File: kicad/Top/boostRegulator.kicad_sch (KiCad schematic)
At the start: 20 parts

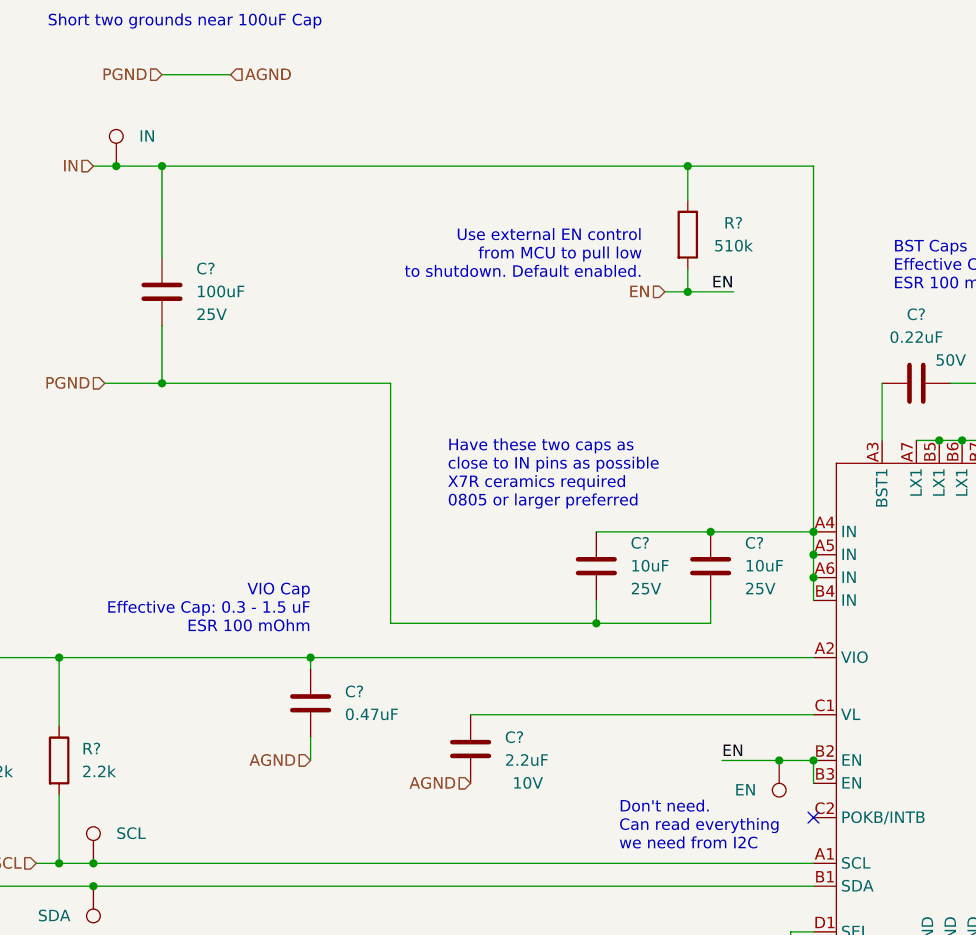
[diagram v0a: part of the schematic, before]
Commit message: Changed boost regulator to default off with MCU to turn on
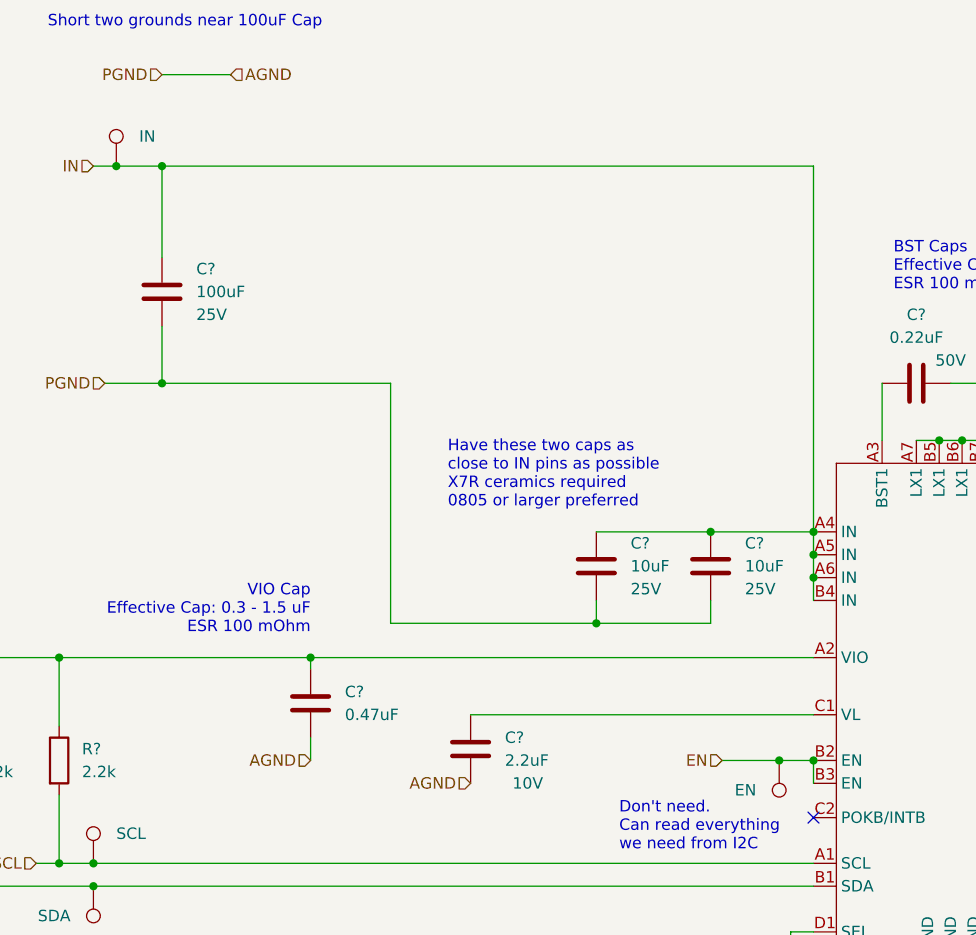
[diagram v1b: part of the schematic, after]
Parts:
- removed R?: 510k, symbol Device:R
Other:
- note removed: "Use external EN control from MCU to pull low to shutdown. Default enabled."
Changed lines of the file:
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@@
   (junction (at 160.02 85.09) (diameter 0) (color 0 0 0 0)
   )
-  (junction (at 132.08 68.58) (diameter 0) (color 0 0 0 0)
-  )
   (junction (at 193.04 100.33) (diameter 0) (color 0 0 0 0)
   )
@@
   )
   (junction (at 193.04 97.79) (diameter 0) (color 0 0 0 0)
-  )
-  (junction (at 132.08 54.61) (diameter 0) (color 0 0 0 0)
   )
   (junction (at 210.82 95.25) (diameter 0) (color 0 0 0 0)
@@
     (stroke (width 0) (type default) (color 0 0 0 0))
   )
-  (wire (pts (xy 132.08 66.04) (xy 132.08 68.58))
-    (stroke (width 0) (type default) (color 0 0 0 0))
-  )
   (wire (pts (xy 146.05 97.79) (xy 146.05 100.33))
     (stroke (width 0) (type default) (color 0 0 0 0))
@@
     (stroke (width 0) (type default) (color 0 0 0 0))
   )
-  (wire (pts (xy 132.08 68.58) (xy 137.16 68.58))
-    (stroke (width 0) (type default) (color 0 0 0 0))
-  )
   (wire (pts (xy 179.07 146.05) (xy 179.07 151.13))
     (stroke (width 0) (type default) (color 0 0 0 0))
   )
-  (wire (pts (xy 132.08 54.61) (xy 132.08 58.42))
-    (stroke (width 0) (type default) (color 0 0 0 0))
-  )
   (wire (pts (xy 146.05 54.61) (xy 146.05 95.25))
     (stroke (width 0) (type default) (color 0 0 0 0))
@@
     (stroke (width 0) (type default) (color 0 0 0 0))
   )
-  (wire (pts (xy 132.08 54.61) (xy 146.05 54.61))
-    (stroke (width 0) (type default) (color 0 0 0 0))
-  )
   (wire (pts (xy 99.06 105.41) (xy 121.92 105.41))
     (stroke (width 0) (type default) (color 0 0 0 0))
@@
     (stroke (width 0) (type default) (color 0 0 0 0))
   )
-  (wire (pts (xy 129.54 68.58) (xy 132.08 68.58))
-    (stroke (width 0) (type default) (color 0 0 0 0))
-  )
   (wire (pts (xy 62.23 116.84) (xy 62.23 109.22))
     (stroke (width 0) (type default) (color 0 0 0 0))
   )
-  (wire (pts (xy 73.66 54.61) (xy 132.08 54.61))
+  (wire (pts (xy 73.66 54.61) (xy 146.05 54.61))
     (stroke (width 0) (type default) (color 0 0 0 0))
   )
@@
     (effects (font (size 1.27 1.27)) (justify left bottom))
   )
-  (text "Use external EN control\nfrom MCU to pull low\nto shutdown. Default enabled."
-    (at 127 67.31 0)
-    (effects (font (size 1.27 1.27)) (justify right bottom))
-  )
   (text "1.08 to 2.0V" (at 34.29 107.95 0)
     (effects (font (size 1.27 1.27)) (justify left bottom))
@@
     (effects (font (size 1.27 1.27)) (justify right bottom))
   )
-  (label "EN" (at 137.16 68.58 180)
-    (effects (font (size 1.27 1.27)) (justify right bottom))
-  )
-  (label "EN" (at 135.89 120.65 0)
-    (effects (font (size 1.27 1.27)) (justify left bottom))
-  )
   (hierarchical_label "OUT" (shape input) (at 250.19 95.25 0)
     (effects (font (size 1.27 1.27)) (justify left))
@@
     (effects (font (size 1.27 1.27)) (justify right))
   )
-  (hierarchical_label "EN" (shape input) (at 129.54 68.58 180)
+  (hierarchical_label "EN" (shape input) (at 135.89 120.65 180)
     (effects (font (size 1.27 1.27)) (justify right))
   )
@@
     (pin "1")
   )
-  (symbol (lib_id "Device:R") (at 132.08 62.23 0) (unit 1)
-    (in_bom yes) (on_board yes)
-    (property "Reference" "R?" (id 0) (at 137.16 60.96 0))
-    (property "Value" "510k" (id 1) (at 137.16 63.5 0))
-    (property "Footprint" "" (id 2) (at 130.302 62.23 90)
-      (effects (font (size 1.27 1.27)) hide)
-    )
-    (property "Datasheet" "~" (id 3) (at 132.08 62.23 0)
-      (effects (font (size 1.27 1.27)) hide)
-    )
-    (pin "1")
-    (pin "2")
-  )
   (symbol (lib_id "Device:C") (at 107.95 119.38 0) (unit 1)

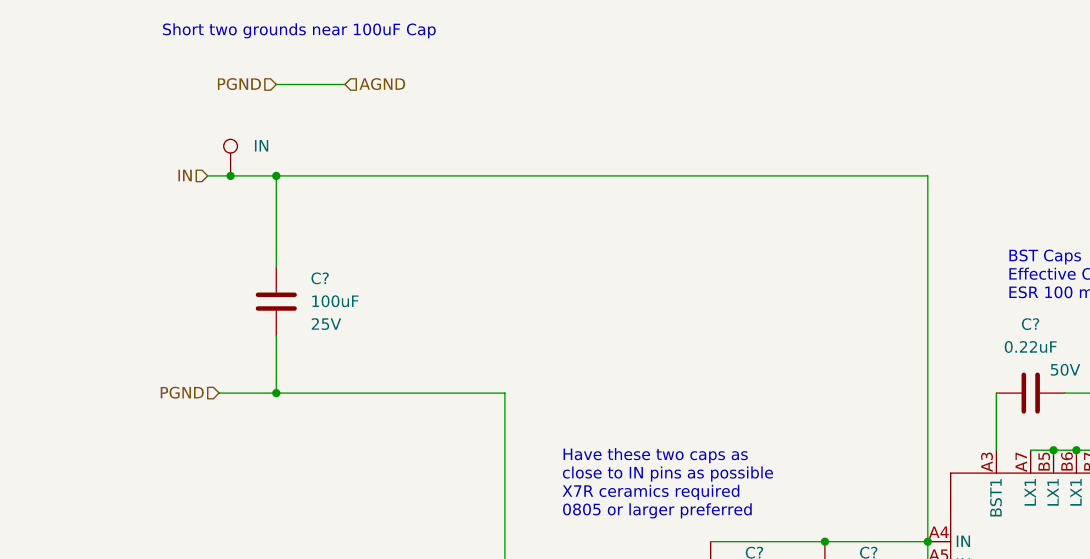
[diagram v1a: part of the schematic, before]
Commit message: Moved GND merge to top sheet
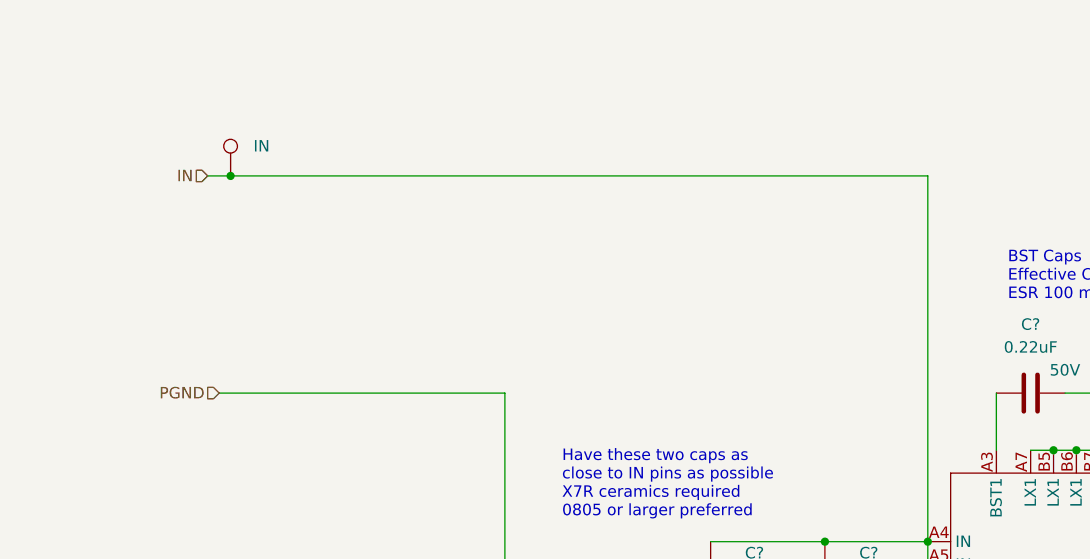
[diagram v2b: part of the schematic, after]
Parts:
- removed C?: 100uF, symbol Device:C
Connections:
- net AGND: no longer C?.1, C?.1, C?.2, C?.2, PGND.1, U?.C3 (PGND), U?.C4 (PGND), U?.C5 (PGND), U?.C6 (PGND), U?.C7 (PGND), U?.D2 (PGND), U?.D3 (PGND)
- new net PGND: C?.1, C?.1, C?.2, C?.2, PGND.1, U?.C3 (PGND), U?.C4 (PGND), U?.C5 (PGND), U?.C6 (PGND), U?.C7 (PGND), U?.D2 (PGND), U?.D3 (PGND)
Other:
- note removed: "Short two grounds near 100uF Cap"
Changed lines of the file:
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@@
   (junction (at 163.83 146.05) (diameter 0) (color 0 0 0 0)
   )
-  (junction (at 73.66 78.74) (diameter 0) (color 0 0 0 0)
-  )
   (junction (at 166.37 78.74) (diameter 0) (color 0 0 0 0)
   )
@@
   )
   (junction (at 193.04 95.25) (diameter 0) (color 0 0 0 0)
-  )
-  (junction (at 73.66 54.61) (diameter 0) (color 0 0 0 0)
   )
   (no_connect (at 146.05 127))
@@
     (stroke (width 0) (type default) (color 0 0 0 0))
   )
-  (wire (pts (xy 73.66 78.74) (xy 73.66 72.39))
-    (stroke (width 0) (type default) (color 0 0 0 0))
-  )
   (wire (pts (xy 143.51 139.7) (xy 143.51 143.51))
     (stroke (width 0) (type default) (color 0 0 0 0))
   )
-  (wire (pts (xy 73.66 44.45) (xy 81.28 44.45))
-    (stroke (width 0) (type default) (color 0 0 0 0))
-  )
   (wire (pts (xy 134.62 95.25) (xy 146.05 95.25))
     (stroke (width 0) (type default) (color 0 0 0 0))
@@
     (stroke (width 0) (type default) (color 0 0 0 0))
   )
-  (wire (pts (xy 73.66 78.74) (xy 99.06 78.74))
+  (wire (pts (xy 67.31 78.74) (xy 99.06 78.74))
     (stroke (width 0) (type default) (color 0 0 0 0))
   )
@@
     (stroke (width 0) (type default) (color 0 0 0 0))
   )
-  (wire (pts (xy 68.58 54.61) (xy 73.66 54.61))
-    (stroke (width 0) (type default) (color 0 0 0 0))
-  )
   (wire (pts (xy 90.17 110.49) (xy 90.17 109.22))
     (stroke (width 0) (type default) (color 0 0 0 0))
@@
     (stroke (width 0) (type default) (color 0 0 0 0))
   )
-  (wire (pts (xy 67.31 78.74) (xy 73.66 78.74))
-    (stroke (width 0) (type default) (color 0 0 0 0))
-  )
   (wire (pts (xy 50.8 109.22) (xy 62.23 109.22))
     (stroke (width 0) (type default) (color 0 0 0 0))
@@
     (stroke (width 0) (type default) (color 0 0 0 0))
   )
-  (wire (pts (xy 73.66 64.77) (xy 73.66 54.61))
-    (stroke (width 0) (type default) (color 0 0 0 0))
-  )
   (wire (pts (xy 99.06 105.41) (xy 121.92 105.41))
     (stroke (width 0) (type default) (color 0 0 0 0))
@@
     (stroke (width 0) (type default) (color 0 0 0 0))
   )
-  (wire (pts (xy 73.66 54.61) (xy 146.05 54.61))
+  (wire (pts (xy 68.58 54.61) (xy 146.05 54.61))
     (stroke (width 0) (type default) (color 0 0 0 0))
   )
@@
     (effects (font (size 1.27 1.27)) (justify left bottom))
   )
-  (text "Short two grounds near 100uF Cap" (at 60.96 39.37 0)
-    (effects (font (size 1.27 1.27)) (justify left bottom))
-  )
   (text "Connect to the output at the point-\nof-load (close to output capacitor)."
     (at 191.77 127 0)
@@
     (effects (font (size 1.27 1.27)) (justify right))
   )
-  (hierarchical_label "PGND" (shape input) (at 73.66 44.45 180)
-    (effects (font (size 1.27 1.27)) (justify right))
-  )
   (hierarchical_label "AGND" (shape input) (at 179.07 151.13 0)
     (effects (font (size 1.27 1.27)) (justify left))
@@
   (hierarchical_label "AGND" (shape input) (at 90.17 120.65 180)
     (effects (font (size 1.27 1.27)) (justify right))
-  )
-  (hierarchical_label "AGND" (shape input) (at 81.28 44.45 0)
-    (effects (font (size 1.27 1.27)) (justify left))
   )
   (hierarchical_label "PGND" (shape input) (at 67.31 78.74 180)
@@
     (pin "1")
   )
-  (symbol (lib_id "Device:C") (at 73.66 68.58 0) (unit 1)
-    (in_bom yes) (on_board yes) (fields_autoplaced)
-    (property "Reference" "C?" (id 0) (at 77.47 66.0399 0)
-      (effects (font (size 1.27 1.27)) (justify left))
-    )
-    (property "Value" "100uF" (id 1) (at 77.47 68.5799 0)
-      (effects (font (size 1.27 1.27)) (justify left))
-    )
-    (property "Footprint" "" (id 2) (at 74.6252 72.39 0)
-      (effects (font (size 1.27 1.27)) hide)
-    )
-    (property "Datasheet" "~" (id 3) (at 73.66 68.58 0)
-      (effects (font (size 1.27 1.27)) hide)
-    )
-    (property "Description" "25V" (id 4) (at 77.47 71.1199 0)
-      (effects (font (size 1.27 1.27)) (justify left))
-    )
-    (pin "1")
-    (pin "2")
-  )
   (symbol (lib_id "Device:C") (at 223.52 99.06 180) (unit 1)

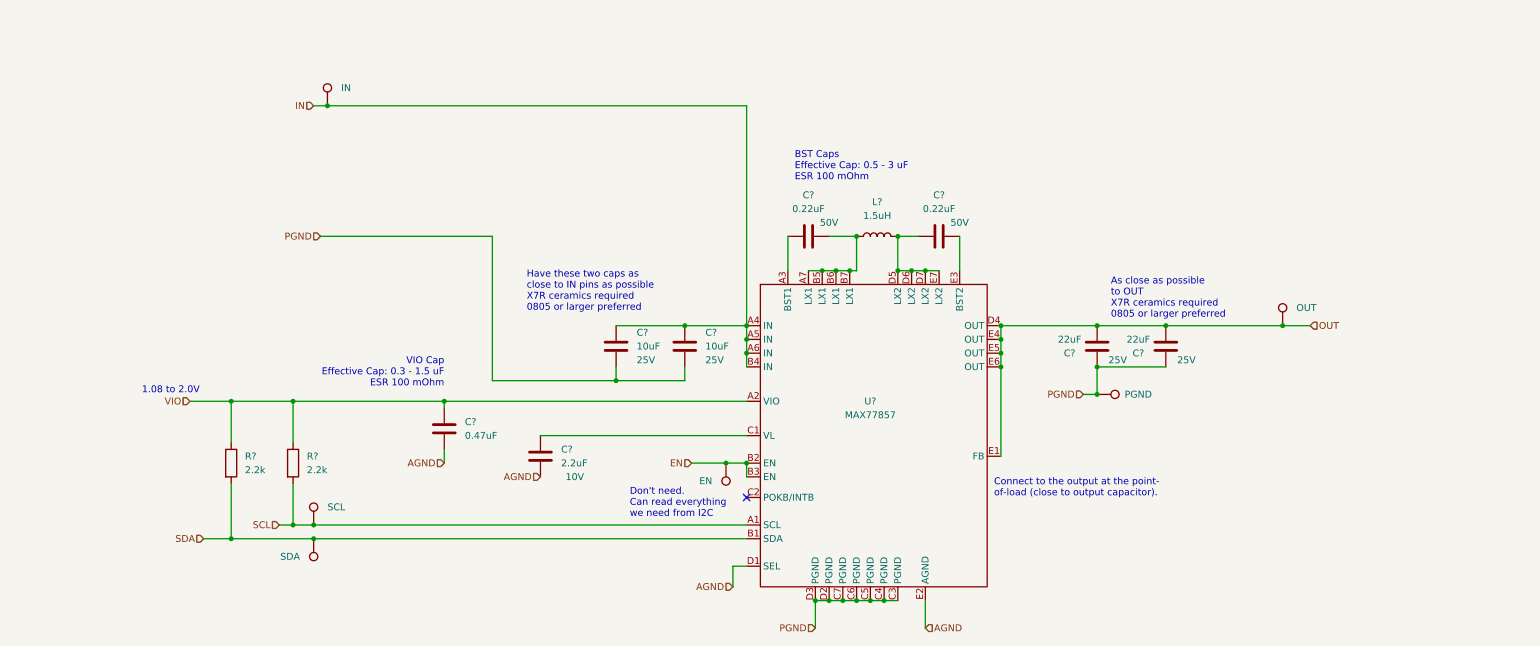
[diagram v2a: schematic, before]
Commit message: Added voltage translation from 3V3 to 1V8
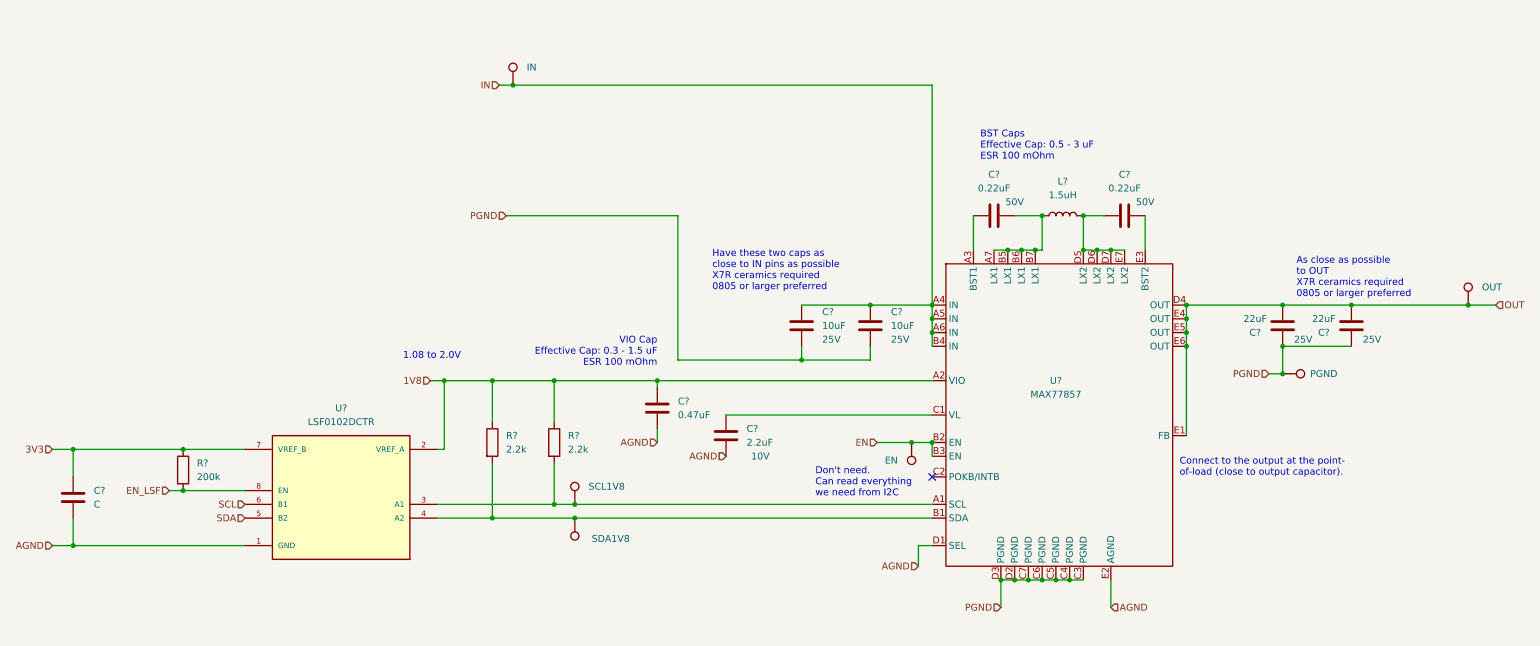
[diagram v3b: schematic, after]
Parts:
- added C?: C, symbol Device:C
- added R?: 200k, symbol Device:R
- added U?: LSF0102DCTR, Snapeda:SOP65P400X130-8N, symbol Logic_LevelTranslator:LSF0102DCTR
- renumbered SCL to SCL1V8, SDA to SDA1V8
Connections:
- net AGND: now also C?.2, U?.1 (GND)
- net SCL: now also U?.6 (B1); no longer R?.2, SCL1V8.1, U?.A1 (SCL)
- net SDA: now also U?.5 (B2); no longer R?.2, SDA1V8.1, U?.B1 (SDA)
- net VIO renamed 1V8
- net 1V8: now also U?.2 (VREF_A)
- new net: R?.2, SCL1V8.1, U?.3 (A1), U?.A1 (SCL)
- new net: R?.2, SDA1V8.1, U?.4 (A2), U?.B1 (SDA)
- new net 3V3: C?.1, R?.1, U?.7 (VREF_B)
- new net EN_LSF: R?.2, U?.8 (EN)
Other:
- moved on the sheet: C?, EN, IN, L?, OUT, PGND, R?, SCL1V8, SDA1V8, U?
